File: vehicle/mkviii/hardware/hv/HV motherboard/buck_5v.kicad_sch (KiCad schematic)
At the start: 15 parts, among them IC601 REG_5A_RT6285GSP

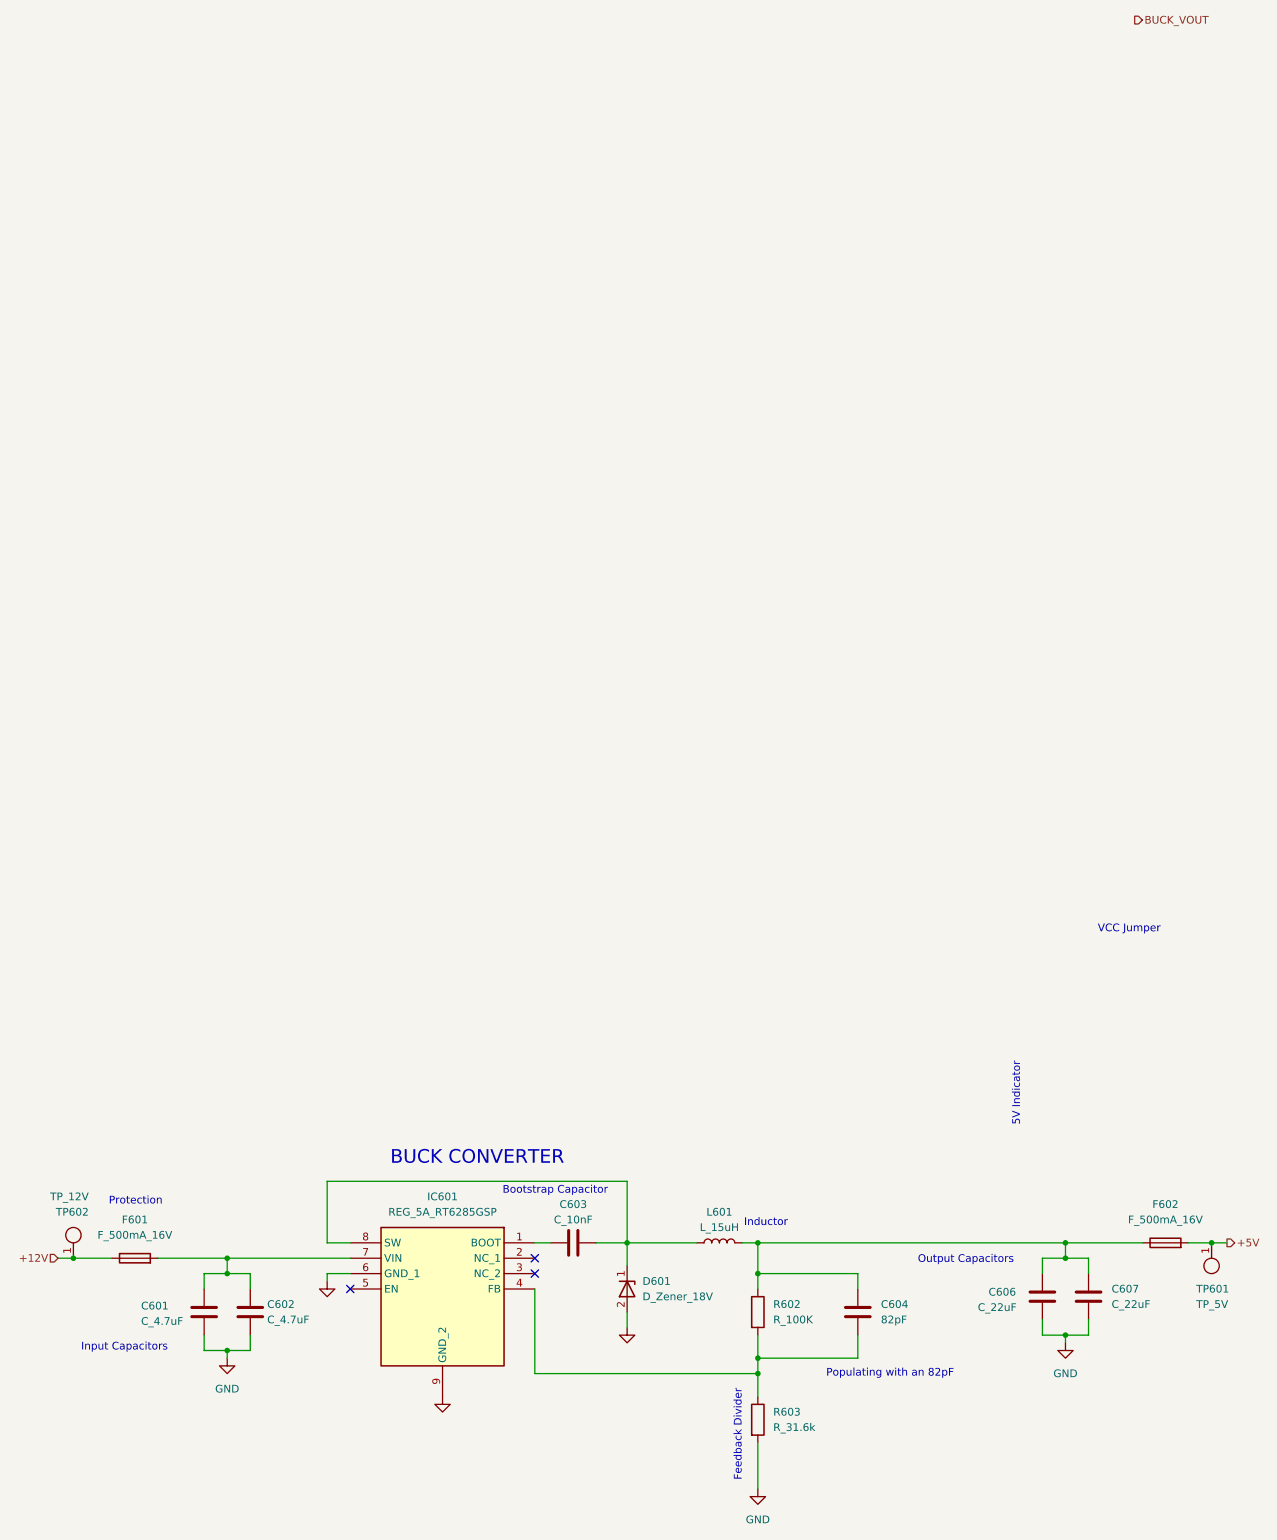
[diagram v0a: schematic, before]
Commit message: added AP63205 buck converter and updated hv motherboard to use it.
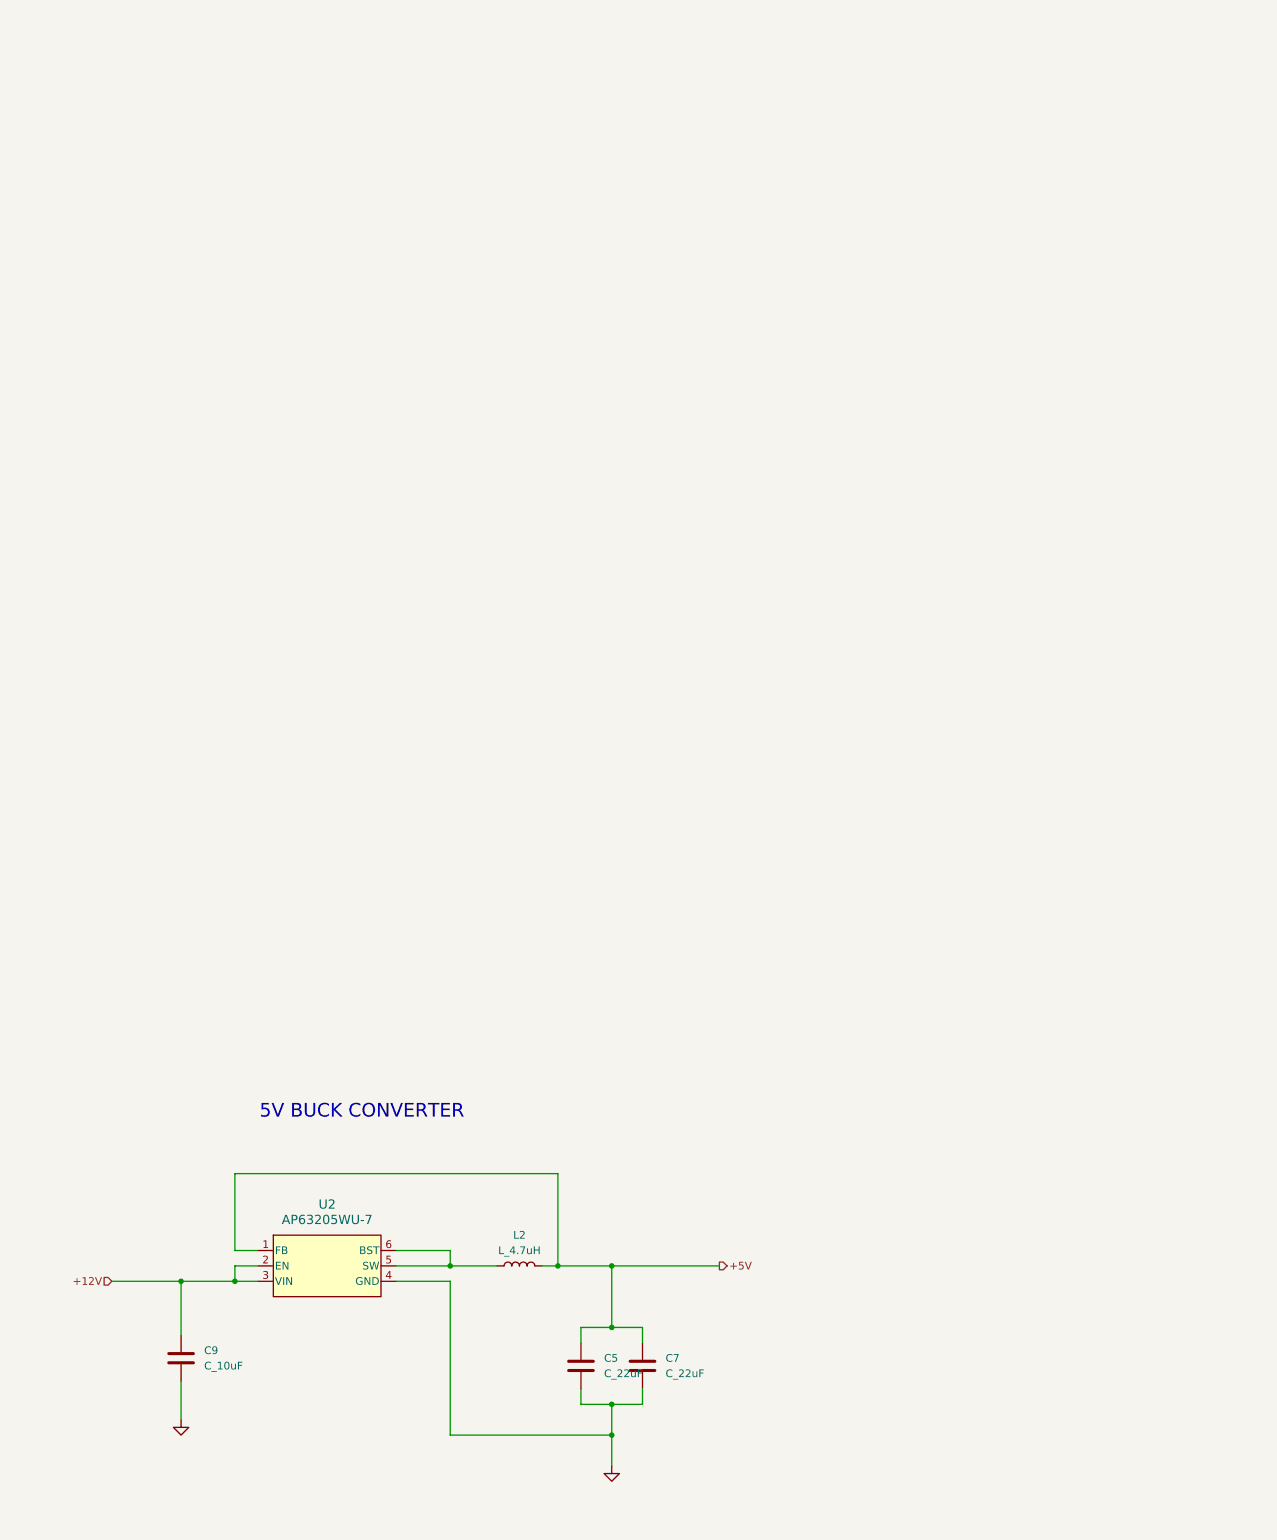
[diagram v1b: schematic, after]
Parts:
- removed C601, C602: C_4.7uF, OEM:C_0603, symbol OEM:C_4.7uF
- removed C603: C_10nF, OEM:C_0603, symbol OEM:C_10nF
- removed C604: 82pF, OEM:C_0603, symbol OEM:100pF
- removed C606, C607: C_22uF, Capacitor_SMD:C_1206_3216Metric, symbol OEM:C_22uF
- removed D601: D_Zener_18V, OEM:DO-214AA, symbol OEM:D_Zener_18V_SMBJ5355B-TP
- removed F601, F602: F_500mA_16V, OEM:Fuse_1210, symbol OEM:F_500mA_16V
- removed IC601: REG_5A_RT6285GSP, OEM:SOIC127P600X175-9N, symbol OEM:REG_5A_RT6285GSP
- removed L601: L_15uH, OEM:NR10050T150M, symbol OEM:L_15uH
- removed R602: R_100K, OEM:R_0603, symbol OEM:R_100K
- removed R603: R_31.6k, OEM:R_0603, symbol OEM:R_75K
- removed TP601: TP_5V, TestPoint:TestPoint_Pad_D1.0mm, symbol OEM:TP_1mm
- removed TP602: TP_12V, TestPoint:TestPoint_Pad_D1.0mm, symbol OEM:TP_1mm
- added C5, C7: C_22uF, Capacitor_SMD:C_1206_3216Metric, symbol OEM:C_22uF_20-100V_1206
- added C9: C_10uF, Capacitor_SMD:C_0603_1608Metric, symbol OEM:C_10uF_0-20V_0603
- added L2: L_4.7uH, OEM:IND_ASPI-4030S-4R7M-T, symbol OEM:L_4.7uH_2A_60m_SMD
- added U2: AP63205WU-7, Package_TO_SOT_SMD:SOT-23-6, symbol OEM:U_5V-Buck-Conv_AP63205WU-7_TSOT23-6
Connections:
- net +12V: now also C9.1, U2.2 (EN), U2.3 (VIN)
- net +5V: now also C5.1, C7.1, L2.2, U2.1 (FB)
- net GND: now also C5.2, C7.2, C9.2, U2.4 (GND)
- new net: L2.1, U2.5 (SW), U2.6 (BST)
- no-connect marks 3 -> 0
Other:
- note added: "5V BUCK CONVERTER"
- note removed: "5V Indicator"
- note removed: "BUCK CONVERTER"
- note removed: "Bootstrap Capacitor"
- note removed: "Feedback Divider"
- note removed: "Inductor"
- note removed: "Input Capacitors"
- note removed: "Output Capacitors"
- note removed: "Populating with an 82pF"
- note removed: "Protection"
- note removed: "VCC Jumper"

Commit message: small changes or smth idk.
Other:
- note added: "Decoupling Capacitor"
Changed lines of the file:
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@@
 	(generator_version "10.0")
 	(paper "A4")
+	(text "Decoupling Capacitor\n"
+		(exclude_from_sim no)
+		(at 85.852 114.554 90)
+		(effects
+			(font
+				(size 1.27 1.27)
+			)
+		)
+	)
 	(text "5V BUCK CONVERTER\n"
 		(exclude_from_sim no)
